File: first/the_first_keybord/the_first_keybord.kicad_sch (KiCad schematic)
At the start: 0 parts

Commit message: 色々更新
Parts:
- added C1: C_Small, symbol Device:C_Small
- added C2, C3, C4, C5: 0.1uf, symbol Device:C_Small
- added C6, C7: 22pF, symbol Device:C_Small
- added R1: 10k, symbol Device:R_Small
- added R2, R3: 22, symbol Device:R_Small
- added R4: 10k, symbol Device:R
- added SW1: SW_Push, symbol Switch:SW_Push
- added U1: ATmega32U4-A, Package_QFP:TQFP-44_10x10mm_P0.8mm, symbol MCU_Microchip_ATmega:ATmega32U4-A
- added Y1: Crystal_GND24_Small, symbol Device:Crystal_GND24_Small
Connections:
- new net: R1.1, U1.33 (~{HWB}/PE2)
- new net: SW1.2, U1.13 (~{RESET})
- new net: C1.1, U1.6 (UCAP)
- new net: C6.2, U1.17 (XTAL1), Y1.1
- new net: C7.2, U1.16 (XTAL2), Y1.3
- new net: R3.2, U1.3 (D-)
- new net: R2.2, U1.4 (D+)
- new net +5V: C2.1, C3.1, C4.1, C5.1, R4.1, U1.14 (VCC), U1.2 (UVCC), U1.24 (AVCC), U1.34 (VCC), U1.44 (AVCC), U1.7 (VBUS)
- new net GND: C1.2, C2.2, C3.2, C4.2, C5.2, C6.1, C7.1, R1.2, SW1.1, U1.15 (GND), U1.23 (GND), U1.35 (GND), U1.43 (GND), U1.5 (UGND), Y1.2 (G), Y1.4 (G)

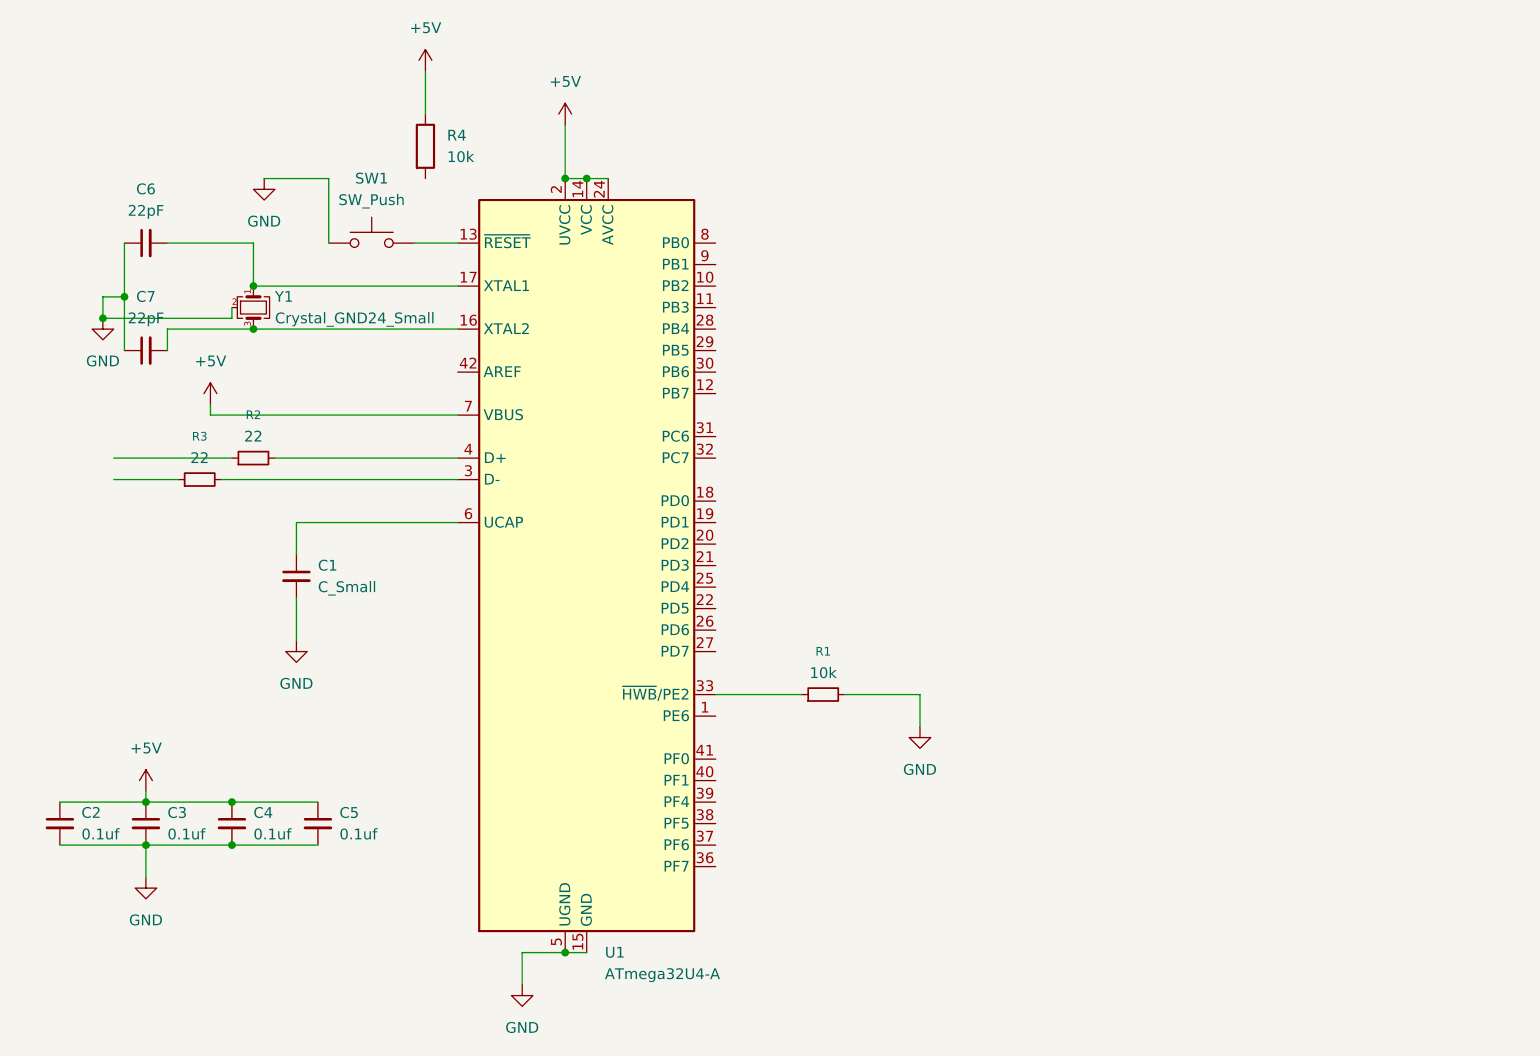
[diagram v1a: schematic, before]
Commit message: フットプリントを割り当て
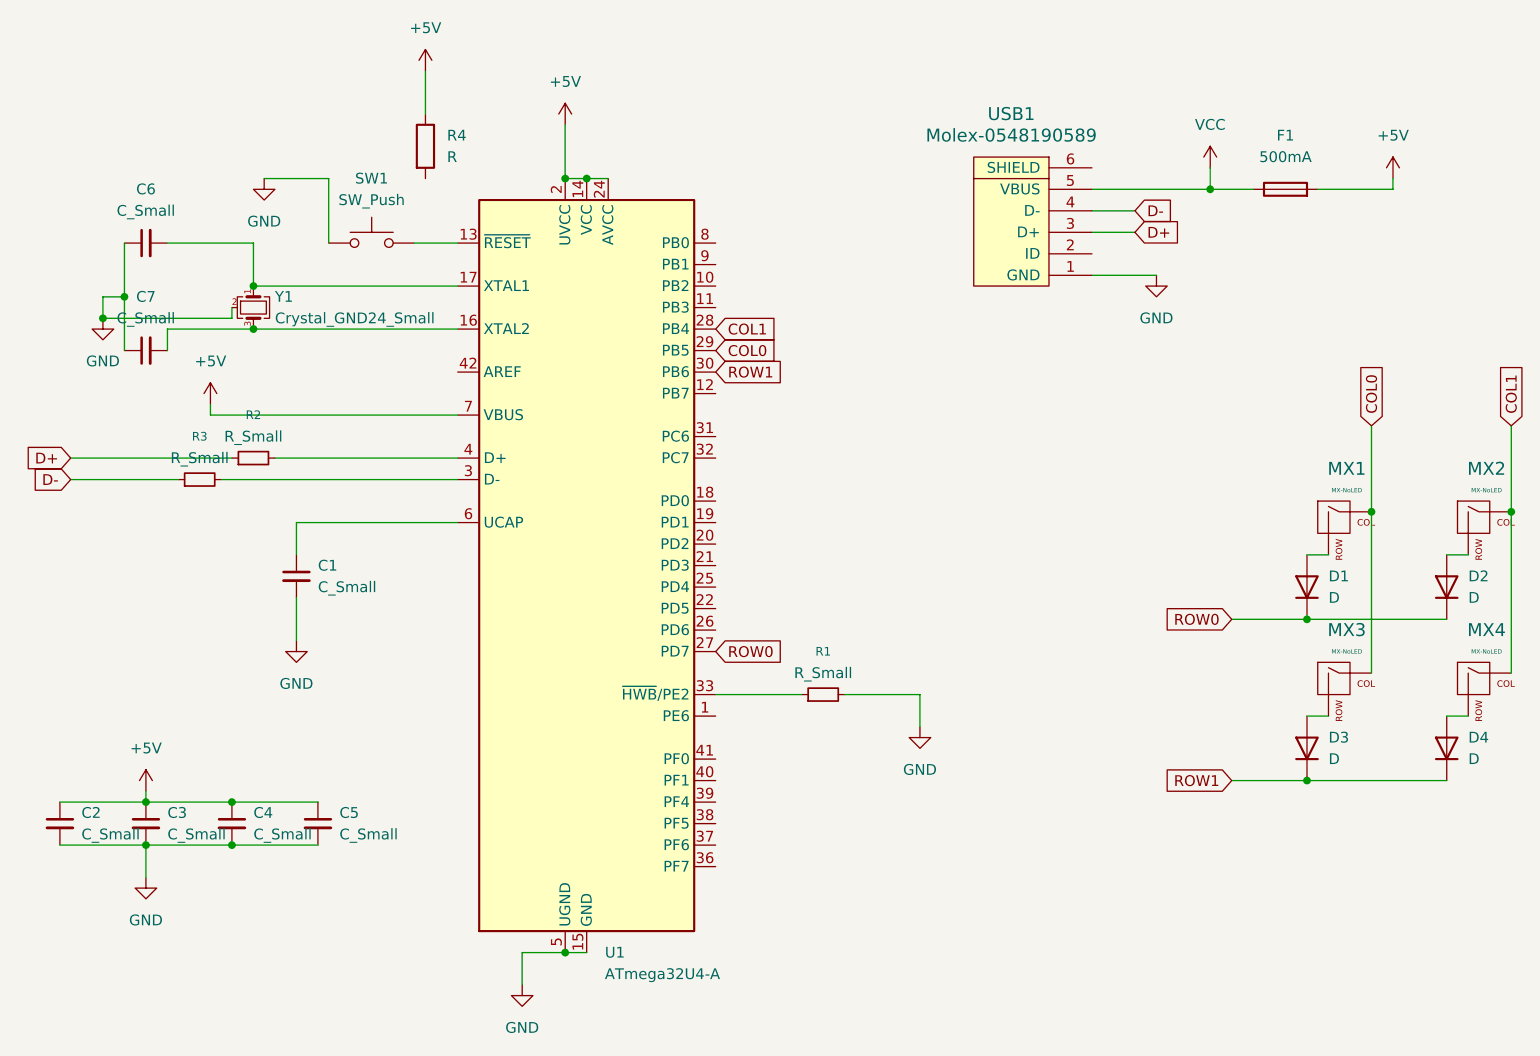
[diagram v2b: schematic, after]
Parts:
- added D1, D2, D3, D4: D, Diode_SMD:D_SOD-123, symbol Device:D
- added F1: 500mA, Fuse:Fuse_1206_3216Metric, symbol Device:Fuse
- added MX1, MX2, MX3, MX4: MX-NoLED, MX_Only:MXOnly-1U-NoLED, symbol MX_Alps_Hybrid:MX-NoLED
- added USB1: Molex-0548190589, random-keyboard-parts:Molex-0548190589, symbol random-keyboard-parts:Molex-0548190589
- C1: footprint (none) -> Capacitor_SMD:C_0805_2012Metric
- C2, C3, C4, C5: value 0.1uf -> C_Small; footprint (none) -> Capacitor_SMD:C_0805_2012Metric
- C6, C7: value 22pF -> C_Small; footprint (none) -> Capacitor_SMD:C_0805_2012Metric
- R1: value 10k -> R_Small; footprint (none) -> Resistor_SMD:R_0805_2012Metric
- R2, R3: value 22 -> R_Small; footprint (none) -> Resistor_SMD:R_0805_2012Metric
- R4: value 10k -> R; footprint (none) -> Resistor_SMD:R_0805_2012Metric
- SW1: footprint (none) -> random-keyboard-parts:SKQG-1155865
- Y1: footprint (none) -> Crystal:Crystal_SMD_3225-4Pin_3.2x2.5mm
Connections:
- net +5V: now also F1.2
- net GND: now also USB1.1 (GND)
- net D-: now reaches R3.1
- net D-: now also USB1.4 (D-)
- net D+: now reaches R2.1
- net D+: now also USB1.3 (D+)
- net ROW0: now reaches U1.27 (PD7)
- net ROW0: now also D1.1 (K), D2.1 (K)
- net COL1: now reaches U1.28 (PB4)
- net COL1: now also MX2.1 (COL), MX4.1 (COL)
- net COL0: now reaches U1.29 (PB5)
- net COL0: now also MX1.1 (COL), MX3.1 (COL)
- net ROW1: now reaches U1.30 (PB6)
- net ROW1: now also D3.1 (K), D4.1 (K)
- new net: D2.2 (A), MX2.2 (ROW)
- new net: D4.2 (A), MX4.2 (ROW)
- new net: D3.2 (A), MX3.2 (ROW)
- new net: D1.2 (A), MX1.2 (ROW)
- new net VCC: F1.1, USB1.5 (VBUS)

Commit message: add keyboard
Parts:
- MX1, MX2, MX3, MX4: footprint MX_Only:MXOnly-1U-NoLED -> MX_Only:MXOnly-1U-Hotswap-Antishear
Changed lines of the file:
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@@
 			)
 		)
-		(property "Footprint" "MX_Only:MXOnly-1U-NoLED"
+		(property "Footprint" "MX_Only:MXOnly-1U-Hotswap-Antishear"
 			(at 175.895 76.835 0)
 			(hide yes)
@@
 			)
 		)
-		(property "Footprint" "MX_Only:MXOnly-1U-NoLED"
+		(property "Footprint" "MX_Only:MXOnly-1U-Hotswap-Antishear"
 			(at 175.895 95.885 0)
 			(hide yes)
@@
 			)
 		)
-		(property "Footprint" "MX_Only:MXOnly-1U-NoLED"
+		(property "Footprint" "MX_Only:MXOnly-1U-Hotswap-Antishear"
 			(at 159.385 76.835 0)
 			(hide yes)
@@
 			)
 		)
-		(property "Footprint" "MX_Only:MXOnly-1U-NoLED"
+		(property "Footprint" "MX_Only:MXOnly-1U-Hotswap-Antishear"
 			(at 159.385 95.885 0)
 			(hide yes)
